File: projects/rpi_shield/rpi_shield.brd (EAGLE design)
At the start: 56 x 65 mm, 10 parts

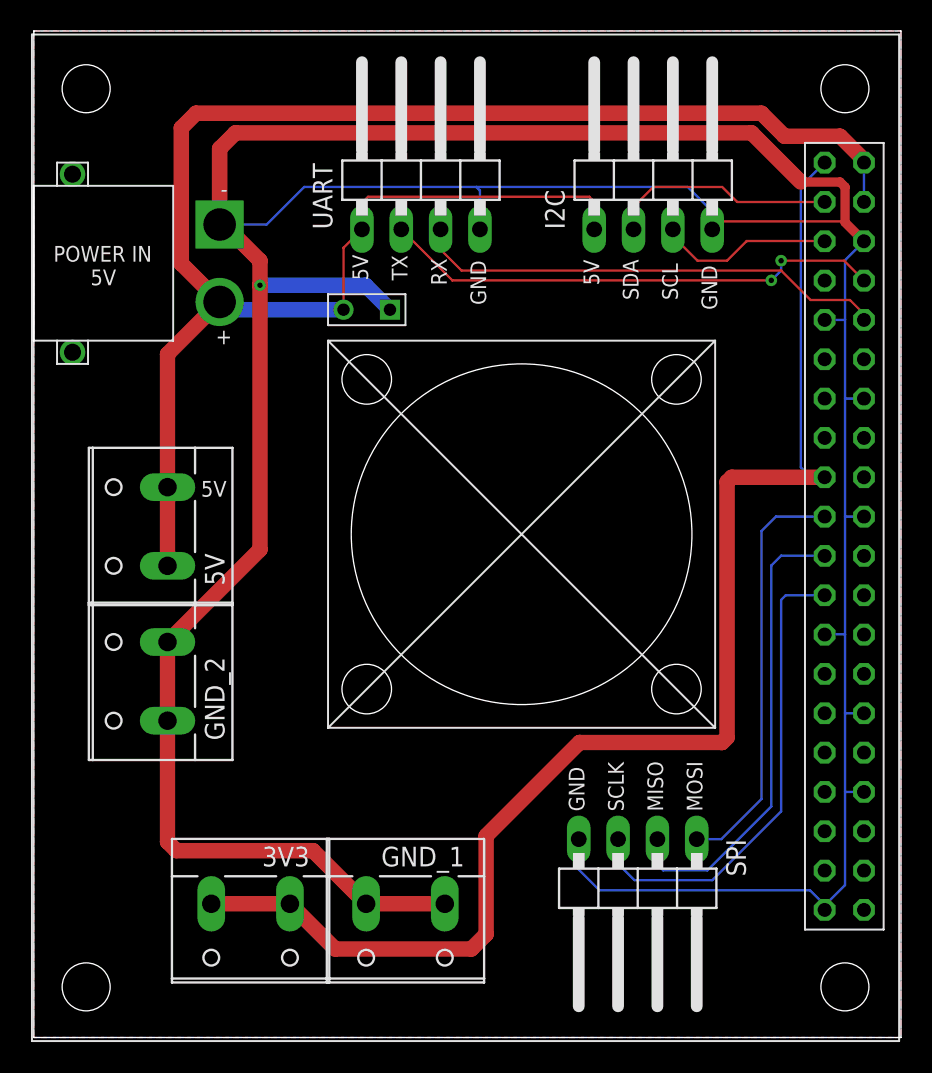
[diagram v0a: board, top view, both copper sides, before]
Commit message: minor fixes of waldek 2 chassis board and rpi shield
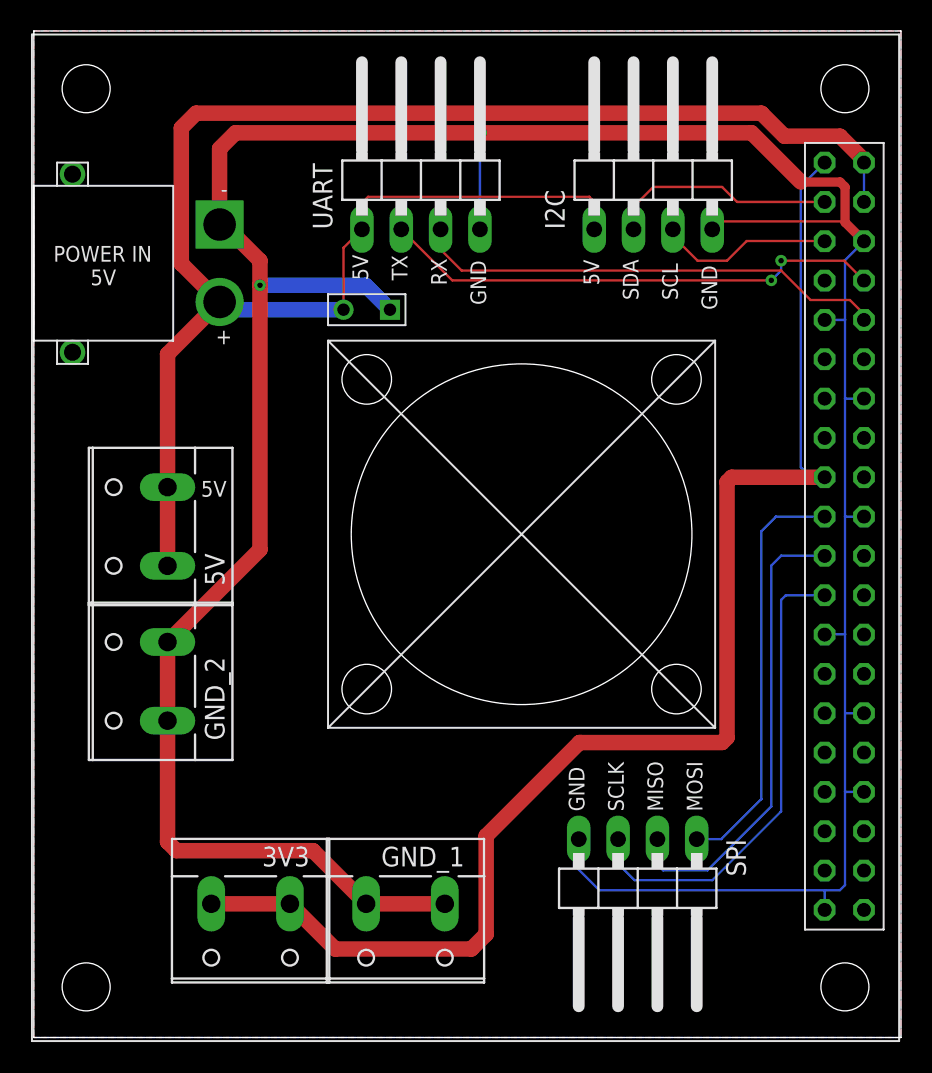
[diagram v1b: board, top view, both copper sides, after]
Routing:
- net GND: track 242.3 -> 211.0 mm, vias 1 -> 2
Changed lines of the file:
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@@
 <contactref element="U$3" pad="PLUS"/>
 <wire x1="53.61" y1="56.5" x2="53.61" y2="53.96" width="0.1524" layer="16"/>
-<wire x1="36.195" y1="53.975" x2="36.19" y2="53.97" width="0.1524" layer="1"/>
 <wire x1="12" y1="47.5" x2="9.525" y2="49.975" width="1" layer="1"/>
 <wire x1="9.525" y1="58.7375" x2="10.4775" y2="59.69" width="1" layer="1"/>
@@
 <contactref element="U$3" pad="MINUS"/>
 <wire x1="53.61" y1="51.42" x2="52.3875" y2="50.1975" width="0.1524" layer="16"/>
-<wire x1="52.3875" y1="9.8425" x2="51.07" y2="8.525" width="0.1524" layer="16"/>
-<wire x1="51.07" y1="8.24" x2="51.07" y2="8.525" width="0.1524" layer="16"/>
 <wire x1="52.3875" y1="50.1975" x2="52.3875" y2="46.355" width="0.1524" layer="16"/>
 <wire x1="52.3875" y1="46.355" x2="52.3875" y2="41.275" width="0.1524" layer="16"/>
@@
 <wire x1="52.3875" y1="26.035" x2="52.3875" y2="20.955" width="0.1524" layer="16"/>
 <wire x1="52.3875" y1="20.955" x2="52.3875" y2="15.875" width="0.1524" layer="16"/>
-<wire x1="52.3875" y1="15.875" x2="52.3875" y2="9.8425" width="0.1524" layer="16"/>
+<wire x1="52.3875" y1="9.8425" x2="52.3875" y2="15.875" width="0.1524" layer="16"/>
 <wire x1="51.07" y1="46.34" x2="52.3725" y2="46.34" width="0.1524" layer="16"/>
 <wire x1="52.3725" y1="46.34" x2="52.3875" y2="46.355" width="0.1524" layer="16"/>
@@
 <wire x1="53.61" y1="15.86" x2="52.4025" y2="15.86" width="0.1524" layer="16"/>
 <wire x1="52.4025" y1="15.86" x2="52.3875" y2="15.875" width="0.1524" layer="16"/>
-<wire x1="51.07" y1="8.24" x2="51.07" y2="8.5575" width="0.1524" layer="16"/>
-<wire x1="51.07" y1="8.5575" x2="50.1175" y2="9.51" width="0.1524" layer="16"/>
-<wire x1="50.1175" y1="9.51" x2="36.5275" y2="9.51" width="0.1524" layer="16"/>
 <wire x1="35.19" y1="10.8475" x2="35.19" y2="12.81" width="0.1524" layer="16"/>
-<wire x1="36.5275" y1="9.51" x2="35.19" y2="10.8475" width="0.1524" layer="16"/>
-<wire x1="12" y1="52.5" x2="15.035" y2="52.5" width="0.1524" layer="16"/>
-<wire x1="15.035" y1="52.5" x2="17.4625" y2="54.9275" width="0.1524" layer="16"/>
-<wire x1="17.4625" y1="54.9275" x2="28.575" y2="54.9275" width="0.1524" layer="16"/>
-<wire x1="28.575" y1="54.9275" x2="42.2275" y2="54.9275" width="0.1524" layer="16"/>
-<wire x1="43.81" y1="53.345" x2="43.81" y2="52.19" width="0.1524" layer="16"/>
-<wire x1="42.2275" y1="54.9275" x2="43.81" y2="53.345" width="0.1524" layer="16"/>
-<wire x1="28.81" y1="52.19" x2="28.81" y2="54.6925" width="0.1524" layer="16"/>
-<wire x1="28.81" y1="54.6925" x2="28.575" y2="54.9275" width="0.1524" layer="16"/>
+<wire x1="35.19" y1="10.8475" x2="36.5275" y2="9.51" width="0.1524" layer="16"/>
 <wire x1="53.61" y1="51.42" x2="52.325" y2="52.705" width="0.1524" layer="1"/>
 <wire x1="44.325" y1="52.705" x2="43.81" y2="52.19" width="0.1524" layer="1"/>
@@
 <wire x1="12" y1="52.5" x2="12" y2="57.4025" width="1" layer="1"/>
 <wire x1="12" y1="57.4025" x2="13.0175" y2="58.42" width="1" layer="1"/>
-<wire x1="13.0175" y1="58.42" x2="46.355" y2="58.42" width="1" layer="1"/>
+<wire x1="13.0175" y1="58.42" x2="28.8925" y2="58.42" width="1" layer="1"/>
+<wire x1="28.8925" y1="58.42" x2="46.355" y2="58.42" width="1" layer="1"/>
 <wire x1="46.355" y1="58.42" x2="49.53" y2="55.245" width="1" layer="1"/>
 <wire x1="49.53" y1="55.245" x2="52.07" y2="55.245" width="0.6" layer="1"/>
@@
 <wire x1="21.4225" y1="48.5775" x2="14.605" y2="48.5775" width="1" layer="16"/>
 <via x="14.605" y="48.5775" extent="1-16" drill="0.35"/>
+<wire x1="28.81" y1="52.19" x2="28.81" y2="58.3375" width="0.1524" layer="16"/>
+<wire x1="28.81" y1="58.3375" x2="28.8925" y2="58.42" width="0.1524" layer="16"/>
+<via x="28.8925" y="58.42" extent="1-16" drill="0.35"/>
+<wire x1="52.055" y1="9.51" x2="52.3875" y2="9.8425" width="0.1524" layer="16"/>
+<wire x1="36.5275" y1="9.51" x2="51.1175" y2="9.51" width="0.1524" layer="16"/>
+<wire x1="51.1175" y1="9.51" x2="52.055" y2="9.51" width="0.1524" layer="16"/>
+<wire x1="51.07" y1="8.24" x2="51.07" y2="9.4625" width="0.1524" layer="16"/>
+<wire x1="51.07" y1="9.4625" x2="51.1175" y2="9.51" width="0.1524" layer="16"/>
 </signal>
 <signal name="SCL">
